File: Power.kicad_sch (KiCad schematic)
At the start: 0 parts

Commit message: Power first iteration
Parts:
- added C?: 470n, symbol Device:C
- added C?: 100n, symbol Device:C
- added C?: 13p, symbol Device:C
- added C?: 1u, symbol Device:C
- added C?: 4.7u, symbol Device:C
- added L?: 39u, symbol Device:L
- added R?: 324k, symbol Device:R
- added R?: 62k, symbol Device:R
- added U?: L7983PUR, symbol L7983PUR:L7983PUR
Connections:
- new net: L?.1, U?.9 (LX)
- new net: C?.2, U?.3 (VCC)
- new net: C?.2, R?.1, R?.2, U?.1 (VOUT/FB)
- new net 12V: C?.1, U?.7 (EN/UVLO), U?.8 (VIN)
- new net 3.3V: C?.1, C?.1, C?.1, L?.2, R?.1, U?.2 (VBIAS)
- new net GND: C?.1, C?.2, C?.2, C?.2, R?.2, U?.10 (GND_1), U?.11 (GND_2), U?.4 (FSW), U?.5 (LNM/~{LCM})
- no-connect marks 0 -> 1

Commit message: Power second iteration
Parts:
- added ?, U?: ST1S06PUR, symbol ST1S06PUR:ST1S06PUR
- added C? (x2): 22u, symbol Device:C
- added C? (x2): 4.7u, symbol Device:C
- added L? (x2): 3.3u, symbol Device:L
- added R? (x2): 21k, symbol Device:R
- added R? (x2): 64.9k, symbol Device:R
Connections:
- net 3.3V: now also C?.1, L?.2, R?.1
- net GND: now also ?.2 (GND), ?.7 (EP), C?.2, C?.2, C?.2, C?.2, R?.2, R?.2, U?.2 (GND), U?.7 (EP)
- new net: ?.1 (VO/VFB), R?.1, R?.2
- new net: L?.1, U?.3 (SW)
- new net: R?.1, R?.2, U?.1 (VO/VFB)
- new net: ?.3 (SW), L?.1
- new net 5V: ?.4 (VIN_SW), ?.5 (VIN_A), ?.6 (INH), C?.1, C?.1, U?.4 (VIN_SW), U?.5 (VIN_A), U?.6 (INH)
- new net V_bridge: C?.1, L?.2, R?.1
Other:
- moved on the sheet: C?, L?, R?, U?

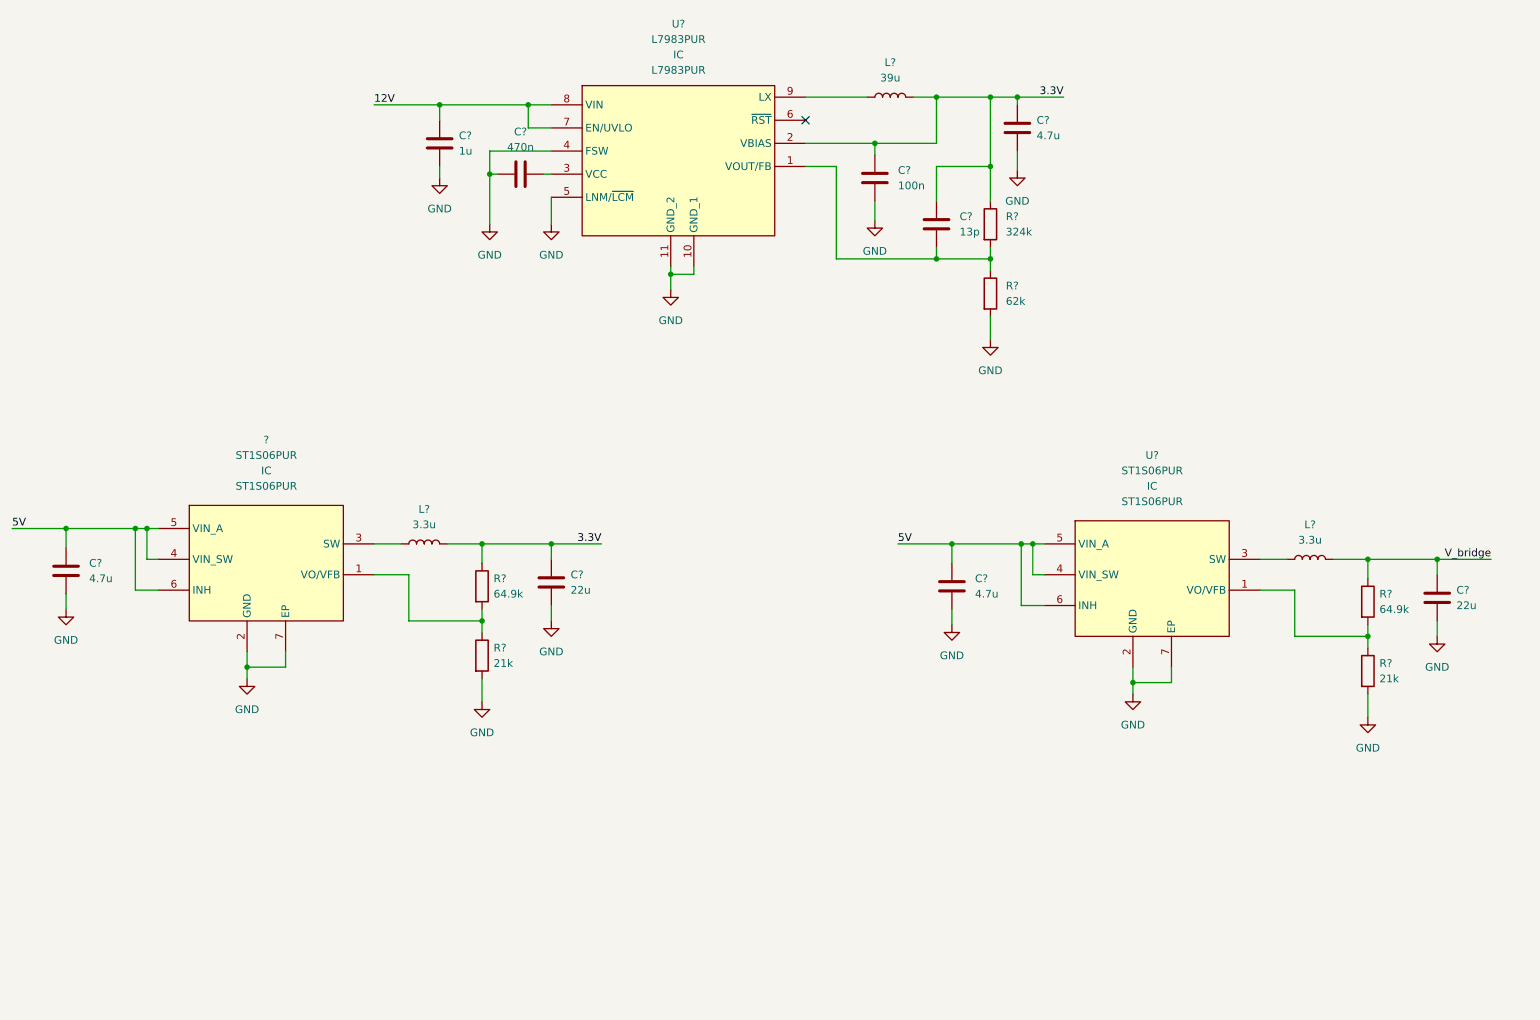
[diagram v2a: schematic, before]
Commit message: MCU_pinout_except_timer please add connector symbols and footprint folder, i will send you parts throughout the day
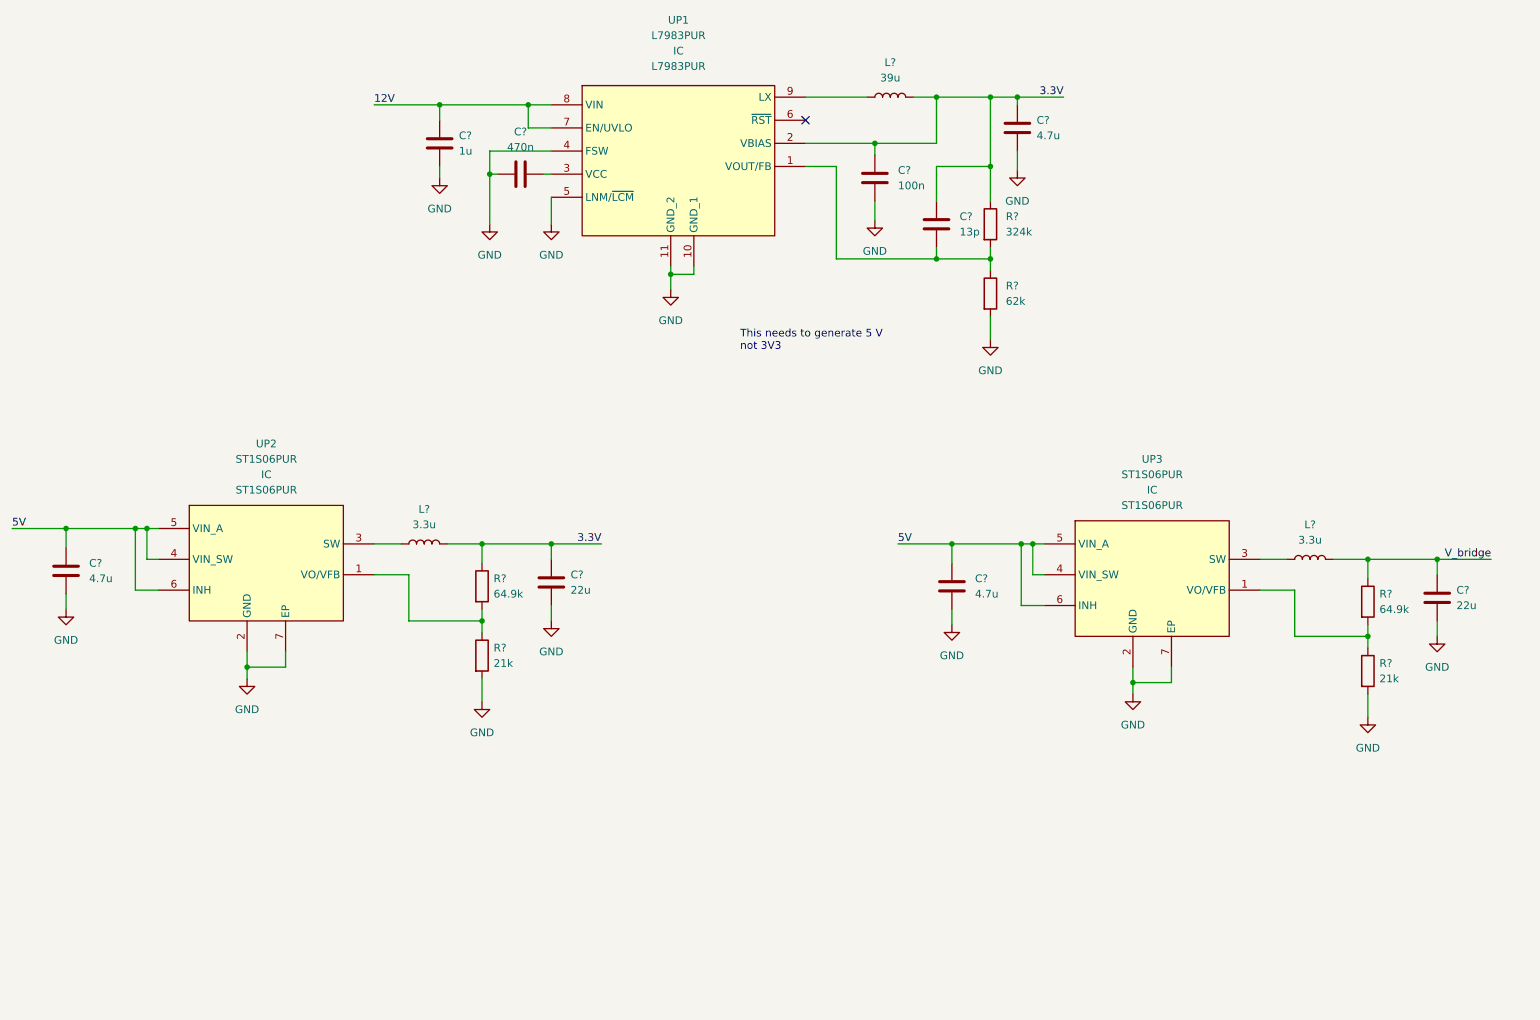
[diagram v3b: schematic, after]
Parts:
- gave numbers to parts that had none: 3
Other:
- note added: "This needs to generate 5 V not 3V3"
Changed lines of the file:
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@@
     (stroke (width 0) (type default) (color 0 0 0 0))
+  )
+  (text "This needs to generate 5 V \nnot 3V3\n" (at 143.51 69.85 0)
+    (effects (font (size 1.27 1.27)) (justify left bottom))
   )
   (label "3.3V" (at 196.85 27.94 180)
@@
   (symbol (lib_id "ST1S06PUR:ST1S06PUR") (at 147.955 104.14 0) (unit 1)
     (in_bom yes) (on_board yes) (fields_autoplaced)
-    (property "Reference" "U?" (id 0) (at 211.455 86.995 0))
-    (property "Value" "ST1S06PUR" (id 1) (at 211.455 89.535 0))
+    (property "Reference" "UP3" (id 0) (at 211.455 87.63 0))
+    (property "Value" "ST1S06PUR" (id 1) (at 211.455 90.17 0))
     (property "Footprint" "" (id 2) (at 229.235 108.585 0)
       (effects (font (size 1.27 1.27)) hide)
@@
       (effects (font (size 1.27 1.27)) hide)
     )
-    (property "Reference_1" "IC" (id 4) (at 211.455 92.075 0))
-    (property "Value_1" "ST1S06PUR" (id 5) (at 211.455 94.615 0))
+    (property "Reference_1" "IC" (id 4) (at 211.455 92.71 0))
+    (property "Value_1" "ST1S06PUR" (id 5) (at 211.455 95.25 0))
     (property "Footprint_1" "SON95P300X300X100-7N-D" (id 6) (at 179.705 199.06 0)
       (effects (font (size 1.27 1.27)) (justify left top) hide)
@@
   (symbol (lib_id "ST1S06PUR:ST1S06PUR") (at 1.905 101.6 0) (unit 1)
     (in_bom yes) (on_board yes) (fields_autoplaced)
-    (property "Reference" "?" (id 0) (at 65.405 84.455 0))
-    (property "Value" "ST1S06PUR" (id 1) (at 65.405 86.995 0))
+    (property "Reference" "UP2" (id 0) (at 65.405 85.09 0))
+    (property "Value" "ST1S06PUR" (id 1) (at 65.405 87.63 0))
     (property "Footprint" "" (id 2) (at 83.185 106.045 0)
       (effects (font (size 1.27 1.27)) hide)
@@
       (effects (font (size 1.27 1.27)) hide)
     )
-    (property "Reference_1" "IC" (id 4) (at 65.405 89.535 0))
-    (property "Value_1" "ST1S06PUR" (id 5) (at 65.405 92.075 0))
+    (property "Reference_1" "IC" (id 4) (at 65.405 90.17 0))
+    (property "Value_1" "ST1S06PUR" (id 5) (at 65.405 92.71 0))
     (property "Footprint_1" "SON95P300X300X100-7N-D" (id 6) (at 33.655 196.52 0)
       (effects (font (size 1.27 1.27)) (justify left top) hide)
@@
   (symbol (lib_id "L7983PUR:L7983PUR") (at 132.715 38.1 0) (unit 1)
     (in_bom yes) (on_board yes) (fields_autoplaced)
-    (property "Reference" "U?" (id 0) (at 133.35 15.875 0))
-    (property "Value" "L7983PUR" (id 1) (at 133.35 18.415 0))
+    (property "Reference" "UP1" (id 0) (at 133.35 15.24 0))
+    (property "Value" "L7983PUR" (id 1) (at 133.35 17.78 0))
     (property "Footprint" "" (id 2) (at 106.299 31.75 0)
       (effects (font (size 1.27 1.27)) hide)
@@
       (effects (font (size 1.27 1.27)) hide)
     )
-    (property "Reference_1" "IC" (id 4) (at 133.35 20.955 0))
-    (property "Value_1" "L7983PUR" (id 5) (at 133.35 23.495 0))
+    (property "Reference_1" "IC" (id 4) (at 133.35 20.32 0))
+    (property "Value_1" "L7983PUR" (id 5) (at 133.35 22.86 0))
     (property "Footprint_1" "L7983PUR" (id 6) (at 167.005 133.02 0)
       (effects (font (size 1.27 1.27)) (justify left top) hide)

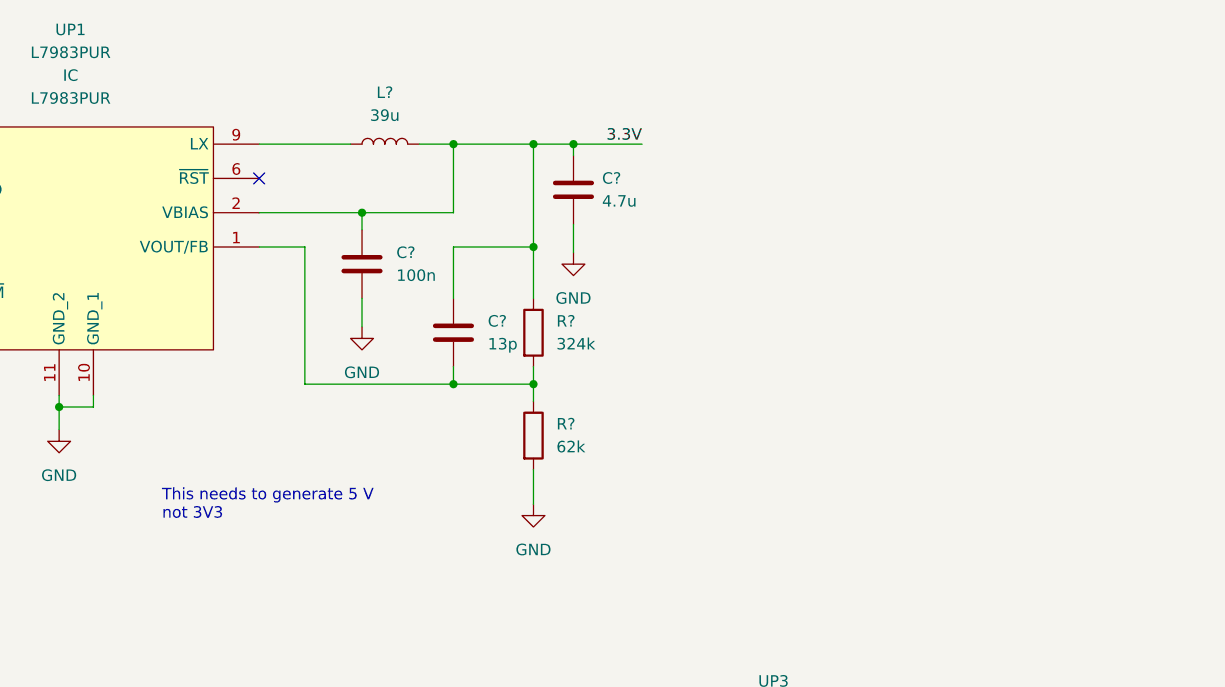
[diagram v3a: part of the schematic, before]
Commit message: Correction in power.sch
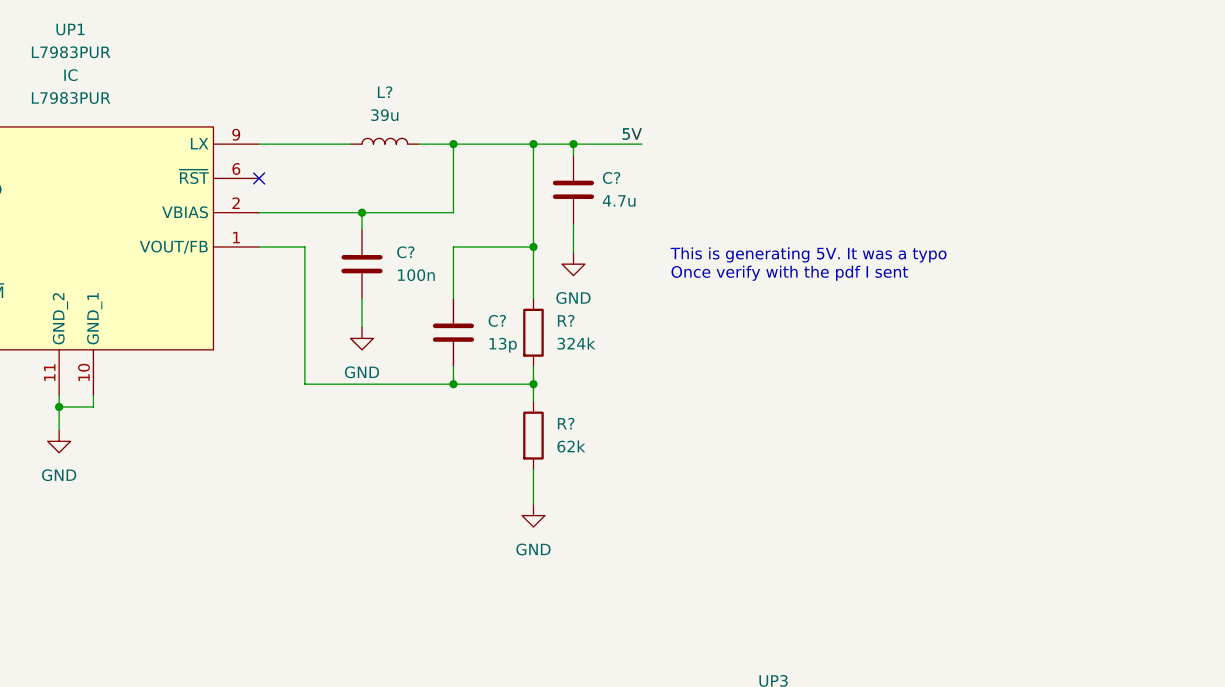
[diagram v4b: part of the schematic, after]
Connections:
- net 3.3V: no longer C?.1, C?.1, C?.1, L?.2, R?.1, UP1.2 (VBIAS)
- net 5V: now also C?.1, C?.1, C?.1, L?.2, R?.1, UP1.2 (VBIAS)
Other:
- note added: "This is generating 5V. It was a typo Once verify with the pdf I sent"
- note removed: "This needs to generate 5 V not 3V3"
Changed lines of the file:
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@@
     (stroke (width 0) (type default) (color 0 0 0 0))
   )
-  (text "This needs to generate 5 V \nnot 3V3\n" (at 143.51 69.85 0)
+  (text "This is generating 5V. It was a typo\nOnce verify with the pdf I sent"
+    (at 200.025 43.18 0)
     (effects (font (size 1.27 1.27)) (justify left bottom))
   )
-  (label "3.3V" (at 196.85 27.94 180)
+  (label "5V" (at 196.85 27.94 180)
     (effects (font (size 1.27 1.27)) (justify right bottom))
   )

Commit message: Motor symbol corrected, Oscillator circuitry added and external footprints added
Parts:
- UP1: footprint (none) -> L7983PUR:L7983PUR
- UP2, UP3: footprint (none) -> ST1S06PUR:SON95P300X300X100-7N-D
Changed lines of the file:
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@@
   (symbol (lib_id "power:GND") (at 32.385 112.395 0) (unit 1)
     (in_bom yes) (on_board yes) (fields_autoplaced)
-    (property "Reference" "#PWR?" (id 0) (at 32.385 118.745 0)
+    (property "Reference" "#PWR0173" (id 0) (at 32.385 118.745 0)
       (effects (font (size 1.27 1.27)) hide)
     )
@@
   (symbol (lib_id "power:GND") (at 247.015 130.175 0) (unit 1)
     (in_bom yes) (on_board yes) (fields_autoplaced)
-    (property "Reference" "#PWR?" (id 0) (at 247.015 136.525 0)
+    (property "Reference" "#PWR0179" (id 0) (at 247.015 136.525 0)
       (effects (font (size 1.27 1.27)) hide)
     )
@@
   (symbol (lib_id "power:GND") (at 189.23 40.005 0) (unit 1)
     (in_bom yes) (on_board yes) (fields_autoplaced)
-    (property "Reference" "#PWR?" (id 0) (at 189.23 46.355 0)
+    (property "Reference" "#PWR0182" (id 0) (at 189.23 46.355 0)
       (effects (font (size 1.27 1.27)) hide)
     )
@@
   (symbol (lib_id "power:GND") (at 165.735 48.26 0) (unit 1)
     (in_bom yes) (on_board yes) (fields_autoplaced)
-    (property "Reference" "#PWR?" (id 0) (at 165.735 54.61 0)
+    (property "Reference" "#PWR0181" (id 0) (at 165.735 54.61 0)
       (effects (font (size 1.27 1.27)) hide)
     )
@@
   (symbol (lib_id "power:GND") (at 112.395 114.3 0) (unit 1)
     (in_bom yes) (on_board yes) (fields_autoplaced)
-    (property "Reference" "#PWR?" (id 0) (at 112.395 120.65 0)
+    (property "Reference" "#PWR0175" (id 0) (at 112.395 120.65 0)
       (effects (font (size 1.27 1.27)) hide)
     )
@@
   (symbol (lib_id "power:GND") (at 62.23 123.825 0) (unit 1)
     (in_bom yes) (on_board yes) (fields_autoplaced)
-    (property "Reference" "#PWR?" (id 0) (at 62.23 130.175 0)
+    (property "Reference" "#PWR0174" (id 0) (at 62.23 130.175 0)
       (effects (font (size 1.27 1.27)) hide)
     )
@@
   (symbol (lib_id "power:GND") (at 93.98 41.275 0) (unit 1)
     (in_bom yes) (on_board yes) (fields_autoplaced)
-    (property "Reference" "#PWR?" (id 0) (at 93.98 47.625 0)
+    (property "Reference" "#PWR0185" (id 0) (at 93.98 47.625 0)
       (effects (font (size 1.27 1.27)) hide)
     )
@@
   (symbol (lib_id "power:GND") (at 184.785 67.945 0) (unit 1)
     (in_bom yes) (on_board yes) (fields_autoplaced)
-    (property "Reference" "#PWR?" (id 0) (at 184.785 74.295 0)
+    (property "Reference" "#PWR0184" (id 0) (at 184.785 74.295 0)
       (effects (font (size 1.27 1.27)) hide)
     )
@@
   (symbol (lib_id "power:GND") (at 132.08 59.69 0) (unit 1)
     (in_bom yes) (on_board yes) (fields_autoplaced)
-    (property "Reference" "#PWR?" (id 0) (at 132.08 66.04 0)
+    (property "Reference" "#PWR0183" (id 0) (at 132.08 66.04 0)
       (effects (font (size 1.27 1.27)) hide)
     )
@@
   (symbol (lib_id "power:GND") (at 178.435 114.935 0) (unit 1)
     (in_bom yes) (on_board yes) (fields_autoplaced)
-    (property "Reference" "#PWR?" (id 0) (at 178.435 121.285 0)
+    (property "Reference" "#PWR0180" (id 0) (at 178.435 121.285 0)
       (effects (font (size 1.27 1.27)) hide)
     )
@@
   (symbol (lib_id "power:GND") (at 102.235 48.895 0) (unit 1)
     (in_bom yes) (on_board yes) (fields_autoplaced)
-    (property "Reference" "#PWR?" (id 0) (at 102.235 55.245 0)
+    (property "Reference" "#PWR0186" (id 0) (at 102.235 55.245 0)
       (effects (font (size 1.27 1.27)) hide)
     )
@@
   (symbol (lib_id "power:GND") (at 100.965 127.635 0) (unit 1)
     (in_bom yes) (on_board yes) (fields_autoplaced)
-    (property "Reference" "#PWR?" (id 0) (at 100.965 133.985 0)
+    (property "Reference" "#PWR0176" (id 0) (at 100.965 133.985 0)
       (effects (font (size 1.27 1.27)) hide)
     )
@@
     (property "Reference" "UP3" (id 0) (at 211.455 87.63 0))
     (property "Value" "ST1S06PUR" (id 1) (at 211.455 90.17 0))
-    (property "Footprint" "" (id 2) (at 229.235 108.585 0)
+    (property "Footprint" "ST1S06PUR:SON95P300X300X100-7N-D" (id 2) (at 229.235 108.585 0)
       (effects (font (size 1.27 1.27)) hide)
     )
@@
     (property "Reference" "UP2" (id 0) (at 65.405 85.09 0))
     (property "Value" "ST1S06PUR" (id 1) (at 65.405 87.63 0))
-    (property "Footprint" "" (id 2) (at 83.185 106.045 0)
+    (property "Footprint" "ST1S06PUR:SON95P300X300X100-7N-D" (id 2) (at 83.185 106.045 0)
       (effects (font (size 1.27 1.27)) hide)
     )
@@
     (property "Reference" "UP1" (id 0) (at 133.35 15.24 0))
     (property "Value" "L7983PUR" (id 1) (at 133.35 17.78 0))
-    (property "Footprint" "" (id 2) (at 106.299 31.75 0)
+    (property "Footprint" "L7983PUR:L7983PUR" (id 2) (at 106.299 31.75 0)
       (effects (font (size 1.27 1.27)) hide)
     )
@@
   (symbol (lib_id "power:GND") (at 112.395 48.895 0) (unit 1)
     (in_bom yes) (on_board yes) (fields_autoplaced)
-    (property "Reference" "#PWR?" (id 0) (at 112.395 55.245 0)
+    (property "Reference" "#PWR0187" (id 0) (at 112.395 55.245 0)
       (effects (font (size 1.27 1.27)) hide)
     )
@@
   (symbol (lib_id "power:GND") (at 258.445 116.84 0) (unit 1)
     (in_bom yes) (on_board yes) (fields_autoplaced)
-    (property "Reference" "#PWR?" (id 0) (at 258.445 123.19 0)
+    (property "Reference" "#PWR0178" (id 0) (at 258.445 123.19 0)
       (effects (font (size 1.27 1.27)) hide)
     )
@@
   (symbol (lib_id "power:GND") (at 208.28 126.365 0) (unit 1)
     (in_bom yes) (on_board yes) (fields_autoplaced)
-    (property "Reference" "#PWR?" (id 0) (at 208.28 132.715 0)
-      (effects (font (size 1.27 1.27)) hide)
-    )
+    (property "Reference" "#PWR0177" (id 0) (at 208.28 132.715 0)
+      (effects (font (size 1.27 1.27)) hide)
+    )
